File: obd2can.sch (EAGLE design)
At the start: 33 parts, among them Q1 8MHz, SW2 6X3.5_TACT, U1 AP3211KTR-G1, U2 SN65HVD235DR, U3 STM32F072-LQFP48, X1 RJ45_RIGHT_ANGLEMOLEX_95001-2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, X2 RJ45_RIGHT_ANGLEMOLEX_95001-2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

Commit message: combined designs together
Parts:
- removed C25, C28: 22uF, rcl:C-USC1206
- removed C27: 10nF, rcl:C-USC0603
- removed D5: (no value), diode:SCHOTTKY-DIODESMC
- removed L1: 4.7uH, rcl:L-EUL2012C
- removed L2: (no value), wuerth-elektronik:WE-CBF_1812
- removed Q1: 8MHz, SparkFun2:CRYSTAL5X3
- removed SV1: (no value), con-lstb:MA06-1
- removed SW2: 6X3.5_TACT, tactile_switch:6X3.5_TACT
- removed TC2: TC2030-IDC-NL, TagConnect:TC2030-IDC-NL
- removed TP2: TPB1,27, testpad:TPB1,27
- removed X1: RJ45_RIGHT_ANGLEMOLEX_95001-2881, FCI_RJ12:RJ45_RIGHT_ANGLEMOLEX_95001-2881
- added C1, C17, C6: 1uF, SparkFun:CAP0402-CAP
- added C1000: 10uF, rcl:CPOL-USSMCA
- added C10000: 1uf, rcl:C-USC0603K
- added C11000, C13000: 22uF, rcl:C-USC1206
- added C13: 560pF, SparkFun:CAP0402-CAP
- added C16: 470pF, SparkFun:CAP0402-CAP
- added C18: 10uF, SparkFun:CAP_POL1206
- added C19: 10nF, rcl:C-USC0603
- added C2000, C6000, C9000: 0.1uf, rcl:C-USC0603K
- added C3000, C7000: 4.7uf, rcl:C-USC0603K
- added C4: 10uF ESR<=5, SparkFun:CAP_POL1206
- added C4000: 0.01uf, rcl:C-USC0603K
- added C8: 4.7uF, SparkFun:CAP0402-CAP
- added D1000: (no value), diode:SCHOTTKY-DIODESMC
- added D2000: 400V 1A, smt_diodes:DIODE1
- added D3: BAS16, SparkFun:DIODESOD
- added D3000: SCHOTTKY, smt_diodes:SCHOTTKY
- added D4: MBRA140, SparkFun:DIODESMA
- added IC1: SCANTOOL, SparkFun:SCANTOOL
- added IC3: LM339PWR, _stn_logic:LM339PWR
- added IC4: MCP2551, _stn_microchip:MCP2551-I/SN
- added JP1: (no value), SparkFun:M08
- added JP8: DNP, SparkFun:FTDI_BASICPTH
- added JP9: DNP, SparkFun:M02PTH
- added L1000: (no value), wuerth-elektronik:WE-CBF_1812
- added L2000: 4.7uH, rcl:L-EUL2012C
- added LED1, LED3: YELLOW, SparkFun:LED0603
- added LED2, LED4, LED5: RED, SparkFun:LED0603
- added Q10, Q9: BSS138, SparkFun:MOSFET-NCHANNELSMD
- added Q1000: 8MHz, SparkFun2:CRYSTAL5X3
- added Q3, Q4, Q8: MMBT2222, SparkFun:TRANSISTOR_NPNSOT23-3
- added Q7: ZXMP6A13FTA, SparkFun:MOSFET-PCHANNEL
- added R10, R12, R18, R21, R27, R28, R29, R30, R31, R33, R9: 10k, SparkFun:RESISTOR0402-RES
- added R1000: 120, rcl:R-US_R0603
- added R11, R8: 510 0.5W, _stn_rcl:R-US_2010
- added R13, R32, R7: 1k, SparkFun:RESISTOR0402-RES
- added R14, R15: 100, SparkFun:RESISTOR0402-RES
- added R16, R23, R25: 4.7k, SparkFun:RESISTOR0402-RES
- added R17: 1.2k, SparkFun:RESISTOR0402-RES
- added R19: 866, SparkFun:RESISTOR0402-RES
- added R20: 240, SparkFun:RESISTOR0402-RES
- added R22: 374, SparkFun:RESISTOR0402-RES
- added R24, R34: 1.5k, SparkFun:RESISTOR0402-RES
- added R26, R5000: 4.7K, rcl:R-US_R0603
- added R3000: 49.9K 1%, rcl:R-US_R0603
- added R35, R37: 330, SparkFun:RESISTOR0402-RES
- added R4000: 16.2K 1%, rcl:R-US_R0603
- added R6: 10K, SparkFun:RESISTOR0402-RES
- added SV1000: (no value), con-lstb:MA06-1
- added SW1: 6X3.5_TACT, tactile_switch:6X3.5_TACT
- added TC1000: TC2030-IDC-NL, TagConnect:TC2030-IDC-NL
- added U1000: SN65HVD235DR, can:MCP2551SO8
- added U2000: STM32F072-LQFP48, stm32f0:STM32F072-LQFP48
- added U3000: AP3211KTR-G1, diodes_inc:AP3211KTR-G1
- added X1000, X2000: RJ45_RIGHT_ANGLEMOLEX_95001-2881, FCI_RJ12:RJ45_RIGHT_ANGLEMOLEX_95001-2881
- added Y1: 16MHz, SparkFun:CRYSTAL5X3
- C10: value 1uf -> 0.1uF; device rcl:C-USC0603K -> SparkFun:CAP0402-CAP
- C11: value 0.01uf -> 1uF; device rcl:C-USC0603K -> SparkFun:CAP0402-CAP
- C12: value 4.7uf -> 560pF; device rcl:C-USC0603K -> SparkFun:CAP0402-CAP
- C14: value 0.1uf -> 0.1uF; device rcl:C-USC0603K -> SparkFun:CAP0402-CAP
- C15: value 4.7uf -> 2.2uF; device rcl:C-USC0603K -> SparkFun:CAP0402-CAP
- C2, C3: value 33pF -> 27pF; device SparkFun:CAP0603 -> SparkFun:CAP0402-CAP
- C5: value 0.1uf -> 1uF; device rcl:C-USC0603K -> SparkFun:CAP0402-CAP
- C7: value 10uF -> 0.1uF; device rcl:CPOL-USSMCA -> SparkFun:CAP0402-CAP
- C9: value 0.1uf -> 10uF; device rcl:C-USC0603K -> SparkFun:CAP_POL1206
- D1: value SCHOTTKY -> BAS16; device smt_diodes:SCHOTTKY -> SparkFun:DIODESOD
- D2: value 400V 1A -> BAS16; device smt_diodes:DIODE1 -> SparkFun:DIODESOD
- R1: value 4.7K -> 10k; device rcl:R-US_R0603 -> SparkFun:RESISTOR0402-RES
- R2: value 120 -> 1k; device rcl:R-US_R0603 -> SparkFun:RESISTOR0402-RES
- R3: value 16.2K 1% -> 62K; device rcl:R-US_R0603 -> SparkFun:RESISTOR0402-RES
- R4: value 49.9K 1% -> 330; device rcl:R-US_R0603 -> SparkFun:RESISTOR0402-RES
- R5: value 4.7K -> 330; device rcl:R-US_R0603 -> SparkFun:RESISTOR0402-RES
- U1: value AP3211KTR-G1 -> 3.3V; device diodes_inc:AP3211KTR-G1 -> SparkFun:V_REG_LDOSMD
- U2: value SN65HVD235DR -> V_REG_317DPACK; device can:MCP2551SO8 -> SparkFun:V_REG_317DPACK
- U3: value STM32F072-LQFP48 -> 5V Reg.; device stm32f0:STM32F072-LQFP48 -> SparkFun:V_REG_LDOSMD
- X2: value RJ45_RIGHT_ANGLEMOLEX_95001-2881 -> Male DB9; device FCI_RJ12:RJ45_RIGHT_ANGLEMOLEX_95001-2881 -> SparkFun:DB9MALE
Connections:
- new net !ISO_K_TX: IC1.!ISO_K_TX, R13.2
- new net !ISO_L_TX: IC1.!ISO_L_TX, R7.2
- new net !ISO_RX: IC1.!ISO_RX, IC3B.OUT, R9.1
- new net !OBD_RX_STATUS!/PGC: IC1.!OBD_RX_LED!/!INT, R4.1
- new net !PWR_SAVE: IC1.PWR_CTRL
- new net !VPW_RX: IC1.!VPW_RX, IC3C.OUT, R18.1
- new net 3.3V: C1.1, C5.1, C8.1, IC1.AVDD, IC1.VDD, LED1.A, LED2.A, LED3.A, LED4.A, R18.2, R27.2, R9.2, U1.OUT
- new net 5V: C11.1, C15.1, C18.+, C6.1, D3.A, IC4.VDD, R1.2, R17.2, R25.1, R34.1, U1.EN, U1.IN, U3.OUT
- new net BATT_V: C7.1, IC1.ANALOG_IN, R3.1, R6.2
- new net CAN_HI: IC4.CANH, JP1.6, R14.2, X2.3
- new net CAN_LO: IC4.CANL, JP1.7, R15.2, X2.5
- new net HOST_PRESENT: IC1.!SLEEP
- new net J1850BUS+: D1.C, JP1.3, R21.1, R28.1, R30.1, X2.7
- new net J1850BUS+_TX: IC1.J1850_BUS+_TX, Q9.G
- new net J1850BUS-: JP1.2, Q8.C, R29.1, R31.2, X2.6
- new net J1850BUS-_TX: IC1.!J1850_BUS-_TX, R32.1
- new net K-LINE: JP1.5, Q4.C, R11.2, R12.1, X2.4
- new net L-LINE: JP1.4, Q3.C, R8.2, X2.8
- new net N$10: C12.1, R14.1
- new net N$11: IC4.RS, R16.2
- new net N$12: IC3C.+IN, R17.1, R23.2
- new net N$13: IC3B.-IN, R12.2
- new net N$14: D3.C, R31.1
- new net N$15: R26.2, U1000G$1.RS
- new net N$16: R3000.2, R4000.1, U3000.FB
- new net N$17: C19.2, U3000.BS
- new net N$18: Q7.G, Q9.D, R24.2
- new net N$19: C19.1, D3000.C, L2000.1, U3000.SW
- new net N$22: Q10.D, R19.1, R22.2
- new net N$24: D2.A, R30.2
- new net N$25: Q8.B, R32.2
- new net N$26: C4.+, IC1.VCAP
- new net N$27: C13.1, R15.1
- new net N$30: LED3.C, R4.2
- new net N$31: LED4.C, R5.1
- new net N$32: LED5.A, R2.1
- new net N$35: LED1.C, R35.2
- new net N$36: LED2.C, R37.1
- new net N$4: Q4.B, R13.1
- new net N$7: IC3C.-IN, R21.2
- new net N$8: R19.2, R20.2, U2.ADJ
- new net N$9: D1.A, Q7.D
- new net OSC1: C2.1, IC1.OSC1, Y1.2
- new net OSC2: C3.1, IC1.OSC2, Y1.1
- new net PWM/!VPW: IC1.PWM/!VPW, Q10.G
- new net PWM_RX: IC1.PWM_RX, IC3A.OUT, R27.1
- new net RST_NVM: IC1.!OBD_TX_LED!/!RST_NVM, JP9.1, R5.2
- new net RX-I: IC1.UART_RX, JP8.3
- new net RX-STAT: IC1.!UART_RX_LED, R35.1
- new net TX-O: IC1.UART_TX, JP8.2, R25.2
- new net TX-STAT: IC1.!UART_TX_LED, R37.2
- new net VBAT: C14.1, D4.C, IC3P.VCC, JP1.8, R10.1, R11.1, R8.1, U2.IN
- new net VBATT_RAW: D4.A, R3.2, X2.9
- new net VCC: C10.1, C17.1, C9.+, Q7.S, R2.2, R20.1, R24.1, U2.OUT, U3.EN, U3.IN
- net +12V: now also L1000.2, X1000.P8, X2000.P8; no longer L2.2, X1.P8, X2.P8
- net +5V: now also SV1000.3; no longer SV1.3
- net AGND: now also U2000.VSSA(P8); no longer U3.VSSA(P8)
- net ANALOG_1_ADC: now also U2000.PA0/USART4_TX/WKUP1/ADC_IN0; no longer U3.PA0/USART4_TX/WKUP1/ADC_IN0
- net CANH: now also R1000.1, U1000G$1.CANH, X1000.P2; no longer R2.1, U2G$1.CANH, X1.P2
- net CANL: now also R1000.2, U1000G$1.CANL, X1000.P3; no longer R2.2, U2G$1.CANL, X1.P3
- net CAN_RX: now also IC1.CAN_RX, IC4.ROUT, U1000G$1.RXD, U2000.PA11/USB_DM/CAN_RX; no longer U2G$1.RXD, U3.PA11/USB_DM/CAN_RX
- net CAN_TX: now also IC1.CAN_TX, IC4.TIN, R34.2, U1000G$1.TXD, U2000.PA12/USB_DP/CAN_TX; no longer U2G$1.TXD, U3.PA12/USB_DP/CAN_TX
- net GND: now also C1.2, C1000.-, C10000.2, C11000.2, C13.2, C13000.2, C16.2, C17.2, C18.-, C2.2, C2000.2, C3.2, C3000.2, C4.-, C4000.2, C6.2, C6000.2, C7.2, C7000.2, C8.2, C9.-, C9000.2, D1000.A, D2.C, D3000.A, IC1.AVSS, IC1.PAD, IC1.VSS@16, IC1.VSS@5, IC3P.GND, IC4.VSS, JP1.1, JP8.6, JP9.2, LED5.C, Q10.S, Q3.E, Q4.E, Q8.E, Q9.S, R16.1, R22.1, R23.1, R26.1, R33.2, R4000.2, R6.1, SV1000.1, SW1.2, TC1000.5, U1000G$1.VREF, U1000G$2.GND, U2000.BOOT0(P44), U2000.VSS_1(P23), U2000.VSS_2(P35), U2000.VSS_3(P47), U3.GND, U3000.GND, X1000.P1, X2.1, X2.2, X2000.P1; no longer C2.1, C25.2, C28.2, C3.1, C7.-, C9.2, D1.A, D5.A, R1.1, R3.2, SV1.1, SW2.2, TC2.5, U2G$1.VREF, U2G$2.GND, U3.BOOT0(P44), U3.VSS_1(P23), U3.VSS_2(P35), U3.VSS_3(P47), X1.P1, X2.P1
- net N$1: now also IC3A.+IN, R28.2; no longer R3.1, R4.2, U1.FB
- net N$3: now also IC3A.-IN, R29.2; no longer TP2.TP, U3.PB0/ADC_IN8/TIM3_CH3
- net N$34: now also C16.1, U3.BP; no longer R1.2, U2G$1.RS
- net N$40: now also Q1000.2, U2000.PF1/OSC_OUT; no longer C2.2, Q1.2, U3.PF1/OSC_OUT
- net N$42: now also Q1000.1, U2000.PF0/OSC_IN; no longer C3.2, Q1.1, U3.PF0/OSC_IN
- net N$5: now also Q3.B, R7.1; no longer C27.2, U1.BS
- net N$50: now also D2000.A, L1000.1; no longer D2.A, L2.1
- net N$6: now also IC3B.+IN, R10.2, R33.1; no longer C27.1, D1.C, L1.1, U1.SW
- net RESET: now also IC1.!RESET, R1.1, R5000.1, SW1.1, TC1000.3, U2000.NRST(P7); no longer R5.1, SW2.1, TC2.3, U3.NRST(P7)
- net SAFE12V: now also C11000.1, D1000.C, D2000.C, U3000.EN, U3000.IN; no longer C25.1, D2.C, D5.C, U1.EN, U1.IN
- net SWCLK: now also TC1000.4, U2000.PA14/USART2_TX/SWCLK; no longer TC2.4, U3.PA14/USART2_TX/SWCLK
- net SWDIO: now also TC1000.2, U2000.PA13/SWDIO; no longer TC2.2, U3.PA13/SWDIO
- net U3: now also R3000.1, R5000.2, TC1000.1; no longer R4.1, R5.2, TC2.1
- net USART1_RX: now also SV1000.4, U2000.PA10/USART1_RX/TIM1_CH3; no longer SV1.4, U3.PA10/USART1_RX/TIM1_CH3
- net USART1_TX: now also SV1000.5, U2000.PA9/USART1_TX/TIM1_CH2; no longer SV1.5, U3.PA9/USART1_TX/TIM1_CH2
- net USART2_RX: now also U2000.PA3/ADC_IN3/COMP2_INP/USART2_RX; no longer U3.PA3/ADC_IN3/COMP2_INP/USART2_RX
- net USART2_TX: now also U2000.PA2/ADC_IN2/WKUP4USART2_TX; no longer U3.PA2/ADC_IN2/WKUP4USART2_TX
- net V+: now also C1000.+, C10000.1, C13000.1, C2000.1, C3000.1, C4000.1, C6000.1, C7000.1, C9000.1, L2000.2, U1000G$2.VCC, U2000.VBATT(P1), U2000.VDDA(P9), U2000.VDDIO2(P36), U2000.VDD_1(P24), U2000.VDD_2(P48); no longer C10.1, C11.1, C12.1, C14.1, C15.1, C28.1, C5.1, C7.+, C9.1, L1.2, U2G$2.VCC, U3.VBATT(P1), U3.VDDA(P9), U3.VDDIO2(P36), U3.VDD_1(P24), U3.VDD_2(P48)
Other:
- note added: "+3.3V Power Supply"
- note added: "AVSS"
- note added: "CAN Transceiver"
- note added: "CAP-868"
- note added: "ISO Transceiver"
- note added: "J1850 Transceiver"
- note added: "Main Controller"
- note added: "New Part: LM339"
- note added: "New Parts: 866, 374"
- note added: "Selectable 5.76V or 7.71V"

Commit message: label adjustment, snapshot image
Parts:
- removed C1000: 10uF, rcl:CPOL-USSMCA
- removed C10000: 1uf, rcl:C-USC0603K
- removed C11000, C13000: 22uF, rcl:C-USC1206
- removed C2000, C6000, C9000: 0.1uf, rcl:C-USC0603K
- removed C3000, C7000: 4.7uf, rcl:C-USC0603K
- removed C4000: 0.01uf, rcl:C-USC0603K
- removed D1000: (no value), diode:SCHOTTKY-DIODESMC
- removed IC3: LM339PWR, _stn_logic:LM339PWR
- removed IC4: MCP2551, _stn_microchip:MCP2551-I/SN
- removed JP1: (no value), SparkFun:M08
- removed JP8: DNP, SparkFun:FTDI_BASICPTH
- removed JP9: DNP, SparkFun:M02PTH
- removed LED4, LED5: RED, SparkFun:LED0603
- removed Q1000: 8MHz, SparkFun2:CRYSTAL5X3
- removed Q9: BSS138, SparkFun:MOSFET-NCHANNELSMD
- removed R1000: 120, rcl:R-US_R0603
- removed R3000: 49.9K 1%, rcl:R-US_R0603
- removed R33: 10k, SparkFun:RESISTOR0402-RES
- removed R34: 1.5k, SparkFun:RESISTOR0402-RES
- removed R35, R37: 330, SparkFun:RESISTOR0402-RES
- removed R4000: 16.2K 1%, rcl:R-US_R0603
- removed R5000: 4.7K, rcl:R-US_R0603
- removed U1000: SN65HVD235DR, can:MCP2551SO8
- removed U3000: AP3211KTR-G1, diodes_inc:AP3211KTR-G1
- removed X2000: RJ45_RIGHT_ANGLEMOLEX_95001-2881, FCI_RJ12:RJ45_RIGHT_ANGLEMOLEX_95001-2881
- added C20, C23: 10uF, SparkFun:CAP_POL1206
- added C21: 2.2uF, SparkFun:CAP0402-CAP
- added C22: 470pF, SparkFun:CAP0402-CAP
- added C24: 0.1uF, SparkFun:CAP0402-CAP
- added IC2: SCANTOOL, SparkFun:SCANTOOL
- added Q5, Q6: MMBT2222, SparkFun:TRANSISTOR_NPNSOT23-3
- added U5: 5V Reg., SparkFun:V_REG_LDOSMD
- C1, C6: value 1uF -> 0.1uF
- C10: value 0.1uF -> 0.1uf; device SparkFun:CAP0402-CAP -> rcl:C-USC0603K
- C11: value 1uF -> 10uF; device SparkFun:CAP0402-CAP -> rcl:CPOL-USSMCA
- C12: value 560pF -> 4.7uf; device SparkFun:CAP0402-CAP -> rcl:C-USC0603K
- C13: value 560pF -> 0.01uf; device SparkFun:CAP0402-CAP -> rcl:C-USC0603K
- C14: value 0.1uF -> 22uF; device SparkFun:CAP0402-CAP -> rcl:C-USC1206
- C15: value 2.2uF -> 10nF; device SparkFun:CAP0402-CAP -> rcl:C-USC0603
- C16: value 470pF -> 0.1uf; device SparkFun:CAP0402-CAP -> rcl:C-USC0603K
- C17: value 1uF -> 4.7uf; device SparkFun:CAP0402-CAP -> rcl:C-USC0603K
- C18: value 10uF -> 22uF; device SparkFun:CAP_POL1206 -> rcl:C-USC1206
- C19: value 10nF -> 1uf; device rcl:C-USC0603 -> rcl:C-USC0603K
- C2: value 27pF -> 1uF
- C7: value 0.1uF -> 27pF
- C8: value 4.7uF -> 1uF
- C9: value 10uF -> 0.1uf; device SparkFun:CAP_POL1206 -> rcl:C-USC0603K
- D4: value MBRA140 -> (none); device SparkFun:DIODESMA -> diode:SCHOTTKY-DIODESMC
- IC1: value SCANTOOL -> LM339PWR; device SparkFun:SCANTOOL -> _stn_logic:LM339PWR
- LED3: value YELLOW -> RED
- Q3: value MMBT2222 -> ZXMP6A13FTA; device SparkFun:TRANSISTOR_NPNSOT23-3 -> SparkFun:MOSFET-PCHANNEL
- Q4: value MMBT2222 -> BSS138; device SparkFun:TRANSISTOR_NPNSOT23-3 -> SparkFun:MOSFET-NCHANNELSMD
- Q7: value ZXMP6A13FTA -> 8MHz; device SparkFun:MOSFET-PCHANNEL -> SparkFun2:CRYSTAL5X3
- R1: value 10k -> 10K
- R10: value 10k -> 374
- R11: value 510 0.5W -> 330; device _stn_rcl:R-US_2010 -> SparkFun:RESISTOR0402-RES
- R13: value 1k -> 1.2k
- R14: value 100 -> 866
- R15: value 100 -> 10k
- R16: value 4.7k -> 240
- R17: value 1.2k -> 10k
- R19: value 866 -> 10k
- R2: value 1k -> 62K
- R20: value 240 -> 120; device SparkFun:RESISTOR0402-RES -> rcl:R-US_R0603
- R21, R27, R28, R9: value 10k -> 1k
- R22: value 374 -> 10k
- R23: value 4.7k -> 10k
- R25: value 4.7k -> 4.7K; device SparkFun:RESISTOR0402-RES -> rcl:R-US_R0603
- R26: value 4.7K -> 510 0.5W; device rcl:R-US_R0603 -> _stn_rcl:R-US_2010
- R29: value 10k -> 49.9K 1%; device SparkFun:RESISTOR0402-RES -> rcl:R-US_R0603
- R3: value 62K -> 10k
- R30: value 10k -> 16.2K 1%; device SparkFun:RESISTOR0402-RES -> rcl:R-US_R0603
- R31: value 10k -> 4.7K; device SparkFun:RESISTOR0402-RES -> rcl:R-US_R0603
- R32: value 1k -> 510 0.5W; device SparkFun:RESISTOR0402-RES -> _stn_rcl:R-US_2010
- R4, R5: value 330 -> 10k
- R6: value 10K -> 10k
- R7: value 1k -> 330
- R8: value 510 0.5W -> 4.7k; device _stn_rcl:R-US_2010 -> SparkFun:RESISTOR0402-RES
- U1: value 3.3V -> V_REG_317DPACK; device SparkFun:V_REG_LDOSMD -> SparkFun:V_REG_317DPACK
- U2: value V_REG_317DPACK -> SN65HVD235DR; device SparkFun:V_REG_317DPACK -> can:MCP2551SO8
- U3: value 5V Reg. -> AP3211KTR-G1; device SparkFun:V_REG_LDOSMD -> diodes_inc:AP3211KTR-G1
- X2: value Male DB9 -> RJ45_RIGHT_ANGLEMOLEX_95001-2881; device SparkFun:DB9MALE -> FCI_RJ12:RJ45_RIGHT_ANGLEMOLEX_95001-2881
- renumbered D2000 to D5, D3000 to D6, L1000 to L1, L2000 to L2, Q10 to Q1, Q8 to Q2, SV1000 to SV1, TC1000 to TC1, U2000 to U4, X1000 to X1
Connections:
- removed net 3.3V: C1.1, C5.1, C8.1, IC1.AVDD, IC1.VDD, LED1.A, LED2.A, LED3.A, LED4.A, R18.2, R27.2, R9.2, U1.OUT
- removed net CAN_HI: IC4.CANH, JP1.6, R14.2, X2.3
- removed net CAN_LO: IC4.CANL, JP1.7, R15.2, X2.5
- removed net N$10: C12.1, R14.1
- removed net N$11: IC4.RS, R16.2
- removed net N$27: C13.1, R15.1
- removed net N$35: LED1.C, R35.2
- removed net N$36: LED2.C, R37.1
- removed net RX-I: IC1.UART_RX, JP8.3
- removed net RX-STAT: IC1.!UART_RX_LED, R35.1
- removed net TX-O: IC1.UART_TX, JP8.2, R25.2
- removed net TX-STAT: IC1.!UART_TX_LED, R37.2
- removed net USART2_RX: U4.PA3/ADC_IN3/COMP2_INP/USART2_RX
- removed net USART2_TX: U4.PA2/ADC_IN2/WKUP4USART2_TX
- removed net VBAT: C14.1, D4.C, IC3P.VCC, JP1.8, R10.1, R11.1, R8.1, U2.IN
- removed net VBATT_RAW: D4.A, R3.2, X2.9
- new net RESET_STN: IC2.!RESET
- new net RX_FROM_STN: IC2.UART_TX, U4.PA3/ADC_IN3/COMP2_INP/USART2_RX
- new net TX_TO_STN: IC2.UART_RX, U4.PA2/ADC_IN2/WKUP4USART2_TX
- net !ISO_K_TX: now also IC2.!ISO_K_TX, R28.2; no longer IC1.!ISO_K_TX, R13.2
- net !ISO_L_TX: now also IC2.!ISO_L_TX, R27.2; no longer IC1.!ISO_L_TX, R7.2
- net !ISO_RX: now also IC1B.OUT, IC2.!ISO_RX, R4.1; no longer IC1.!ISO_RX, IC3B.OUT, R9.1
- net !OBD_RX_STATUS!/PGC: now also IC2.!OBD_RX_LED!/!INT, R7.1; no longer IC1.!OBD_RX_LED!/!INT, R4.1
- net !PWR_SAVE: now also IC2.PWR_CTRL; no longer IC1.PWR_CTRL
- net !VPW_RX: now also IC1C.OUT, IC2.!VPW_RX, R5.1; no longer IC1.!VPW_RX, IC3C.OUT, R18.1
- net +12V: now also R2.2, X2.P8; no longer X2000.P8
- net 5V: now also C20.+, C21.1, D1.A, R13.2, U5.OUT; no longer C11.1, C15.1, C18.+, C6.1, D3.A, IC4.VDD, R1.2, R17.2, R25.1, R34.1, U1.EN, U1.IN, U3.OUT
- net BATT_V: now also C1.1, IC2.ANALOG_IN, R1.2, R2.1; no longer C7.1, IC1.ANALOG_IN, R3.1, R6.2
- net CANH: now also R20.1, U2G$1.CANH; no longer R1000.1, U1000G$1.CANH
- net CANL: now also R20.2, U2G$1.CANL; no longer R1000.2, U1000G$1.CANL
- net CAN_RX: now also U2G$1.RXD; no longer IC1.CAN_RX, IC4.ROUT, U1000G$1.RXD
- net CAN_TX: now also U2G$1.TXD; no longer IC1.CAN_TX, IC4.TIN, R34.2, U1000G$1.TXD
- net GND: now also C11.-, C18.2, C19.2, C20.-, C21.2, C22.2, C23.-, C24.2, C9.2, D4.A, IC1P.GND, IC2.AVSS, IC2.PAD, IC2.VSS@16, IC2.VSS@5, LED2.C, Q4.S, Q5.E, Q6.E, R1.1, R10.1, R15.2, R25.1, R30.2, R8.1, U2G$1.VREF, U2G$2.GND, U5.GND, X2.P1; no longer C1000.-, C10000.2, C11.2, C11000.2, C13000.2, C15.2, C18.-, C2000.2, C3000.2, C4000.2, C6000.2, C7000.2, C9.-, C9000.2, D1000.A, IC1.AVSS, IC1.PAD, IC1.VSS@16, IC1.VSS@5, IC3P.GND, IC4.VSS, JP1.1, JP8.6, JP9.2, LED5.C, Q3.E, Q4.E, Q9.S, R16.1, R22.1, R23.1, R26.1, R33.2, R4000.2, R6.1, U1.GND, U1000G$1.VREF, U1000G$2.GND, U3000.GND, X2.1, X2.2, X2000.P1
- net HOST_PRESENT: now also IC2.!SLEEP; no longer IC1.!SLEEP
- net J1850BUS+: now also D3.C, R18.1, R19.1, R23.1, X2.P4; no longer D1.C, JP1.3, R21.1, R28.1, R30.1, X2.7
- net J1850BUS+_TX: now also IC2.J1850_BUS+_TX, Q4.G; no longer IC1.J1850_BUS+_TX, Q9.G
- net J1850BUS-: now also R17.1, R22.2, X2.P5; no longer JP1.2, R29.1, R31.2, X2.6
- net J1850BUS-_TX: now also IC2.!J1850_BUS-_TX, R21.1; no longer IC1.!J1850_BUS-_TX, R32.1
- net K-LINE: now also Q6.C, R32.2, R6.1, X2.P7; no longer JP1.5, Q4.C, R11.2, R12.1, X2.4
- net L-LINE: now also Q5.C, R26.2, X2.P6; no longer JP1.4, Q3.C, R8.2, X2.8
- net N$1: now also IC1A.+IN, R18.2; no longer IC3A.+IN, R28.2
- net N$12: now also IC1C.+IN, R13.1, R8.2; no longer IC3C.+IN, R17.1, R23.2
- net N$13: now also IC1B.-IN, R6.2; no longer IC3B.-IN, R12.2
- net N$14: now also D1.C, R22.1; no longer D3.C, R31.1
- net N$15: now also R25.2, U2G$1.RS; no longer R26.2, U1000G$1.RS
- net N$16: now also R29.2, R30.1, U3.FB; no longer R3000.2, R4000.1, U3000.FB
- net N$17: now also C15.2, U3.BS; no longer C19.2, U3000.BS
- net N$18: now also Q3.G, Q4.D; no longer Q7.G, Q9.D
- net N$19: now also C15.1, U3.SW; no longer C19.1, U3000.SW
- net N$22: now also R10.2, R14.1; no longer R19.1, R22.2
- net N$24: now also R23.2; no longer R30.2
- net N$25: now also R21.2; no longer R32.2
- net N$26: now also IC2.VCAP; no longer IC1.VCAP
- net N$3: now also IC1A.-IN, R17.2; no longer IC3A.-IN, R29.2
- net N$30: now also LED1.C, R7.2; no longer LED3.C, R4.2
- net N$31: now also LED3.C, R11.1; no longer LED4.C, R5.1
- net N$32: now also LED2.A, R9.1; no longer LED5.A, R2.1
- net N$34: now also C22.1, U5.BP; no longer C16.1, U3.BP
- net N$4: now also Q6.B, R28.1; no longer Q4.B, R13.1
- net N$40: now also Q7.2; no longer Q1000.2
- net N$42: now also Q7.1; no longer Q1000.1
- net N$5: now also Q5.B, R27.1; no longer Q3.B, R7.1
- net N$6: now also IC1B.+IN, R12.2, R15.1; no longer IC3B.+IN, R10.2, R33.1
- net N$7: now also IC1C.-IN, R19.2; no longer IC3C.-IN, R21.2
- net N$8: now also R14.2, R16.2, U1.ADJ; no longer R19.2, R20.2, U2.ADJ
- net N$9: now also D3.A, Q3.D; no longer D1.A, Q7.D
- net OSC1: now also C3.1, IC2.OSC1; no longer C2.1, IC1.OSC1
- net OSC2: now also C7.1, IC2.OSC2; no longer C3.1, IC1.OSC2
- net PWM/!VPW: now also IC2.PWM/!VPW; no longer IC1.PWM/!VPW
- net PWM_RX: now also IC1A.OUT, IC2.PWM_RX, R3.1; no longer IC1.PWM_RX, IC3A.OUT, R27.1
- net RESET: now also R31.1; no longer IC1.!RESET, R1.1, R5000.1
- net RST_NVM: now also IC2.!OBD_TX_LED!/!RST_NVM, R11.2; no longer IC1.!OBD_TX_LED!/!RST_NVM, JP9.1, R5.2
- net SAFE12V: now also C14.1, C6.1, D4.C, IC1P.VCC, R12.1, R26.1, R32.1, U1.IN, U3.EN, U3.IN; no longer C11000.1, D1000.C, U3000.EN, U3000.IN
- net U3: now also R29.1, R31.2; no longer R3000.1, R5000.2
- net V+: now also C10.1, C11.+, C12.1, C13.1, C16.1, C17.1, C18.1, C19.1, C2.1, C8.1, C9.1, IC2.AVDD, IC2.VDD, LED1.A, LED3.A, R3.2, R4.2, R5.2, U2G$2.VCC; no longer C1000.+, C10000.1, C13000.1, C2000.1, C3000.1, C4000.1, C6000.1, C7000.1, C9000.1, U1000G$2.VCC
- net VCC: now also C23.+, C24.1, C5.1, Q3.S, R16.1, R9.2, U1.OUT, U5.EN, U5.IN; no longer C10.1, C17.1, C9.+, Q7.S, R2.2, R20.1, U2.OUT, U3.EN, U3.IN
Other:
- note removed: "CAN Transceiver"

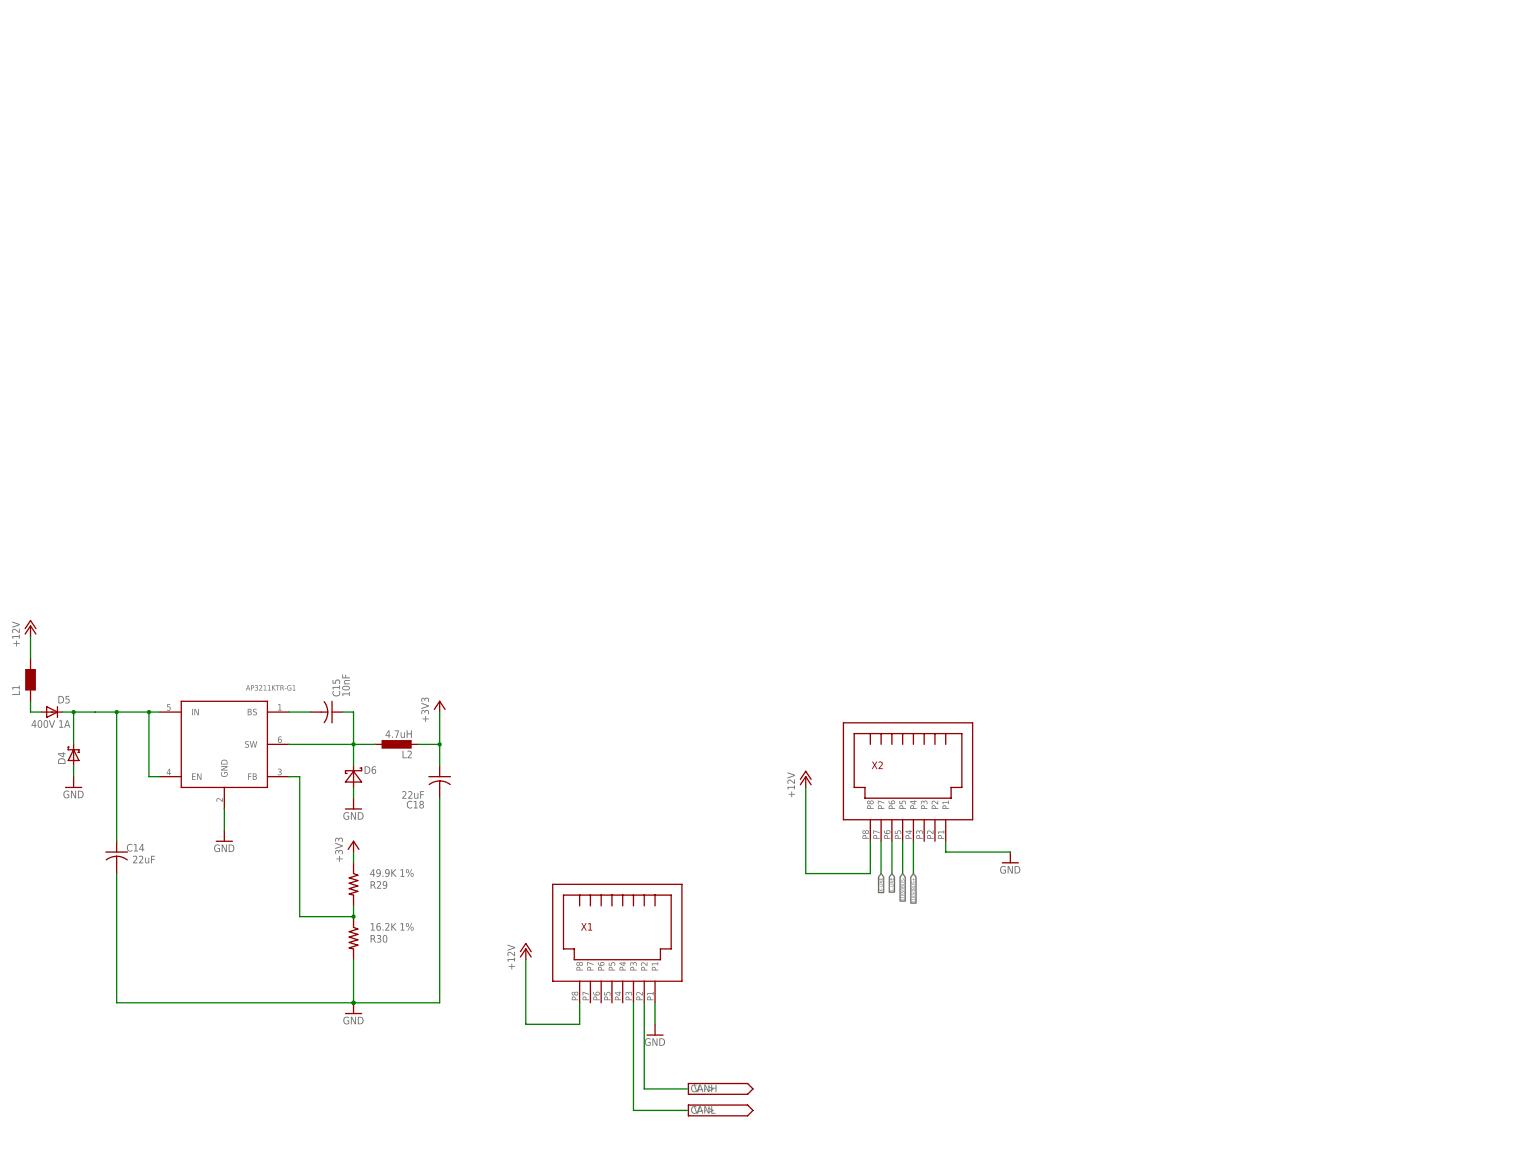
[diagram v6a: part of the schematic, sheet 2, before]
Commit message: OBD2CAN WIP - more air wires routed
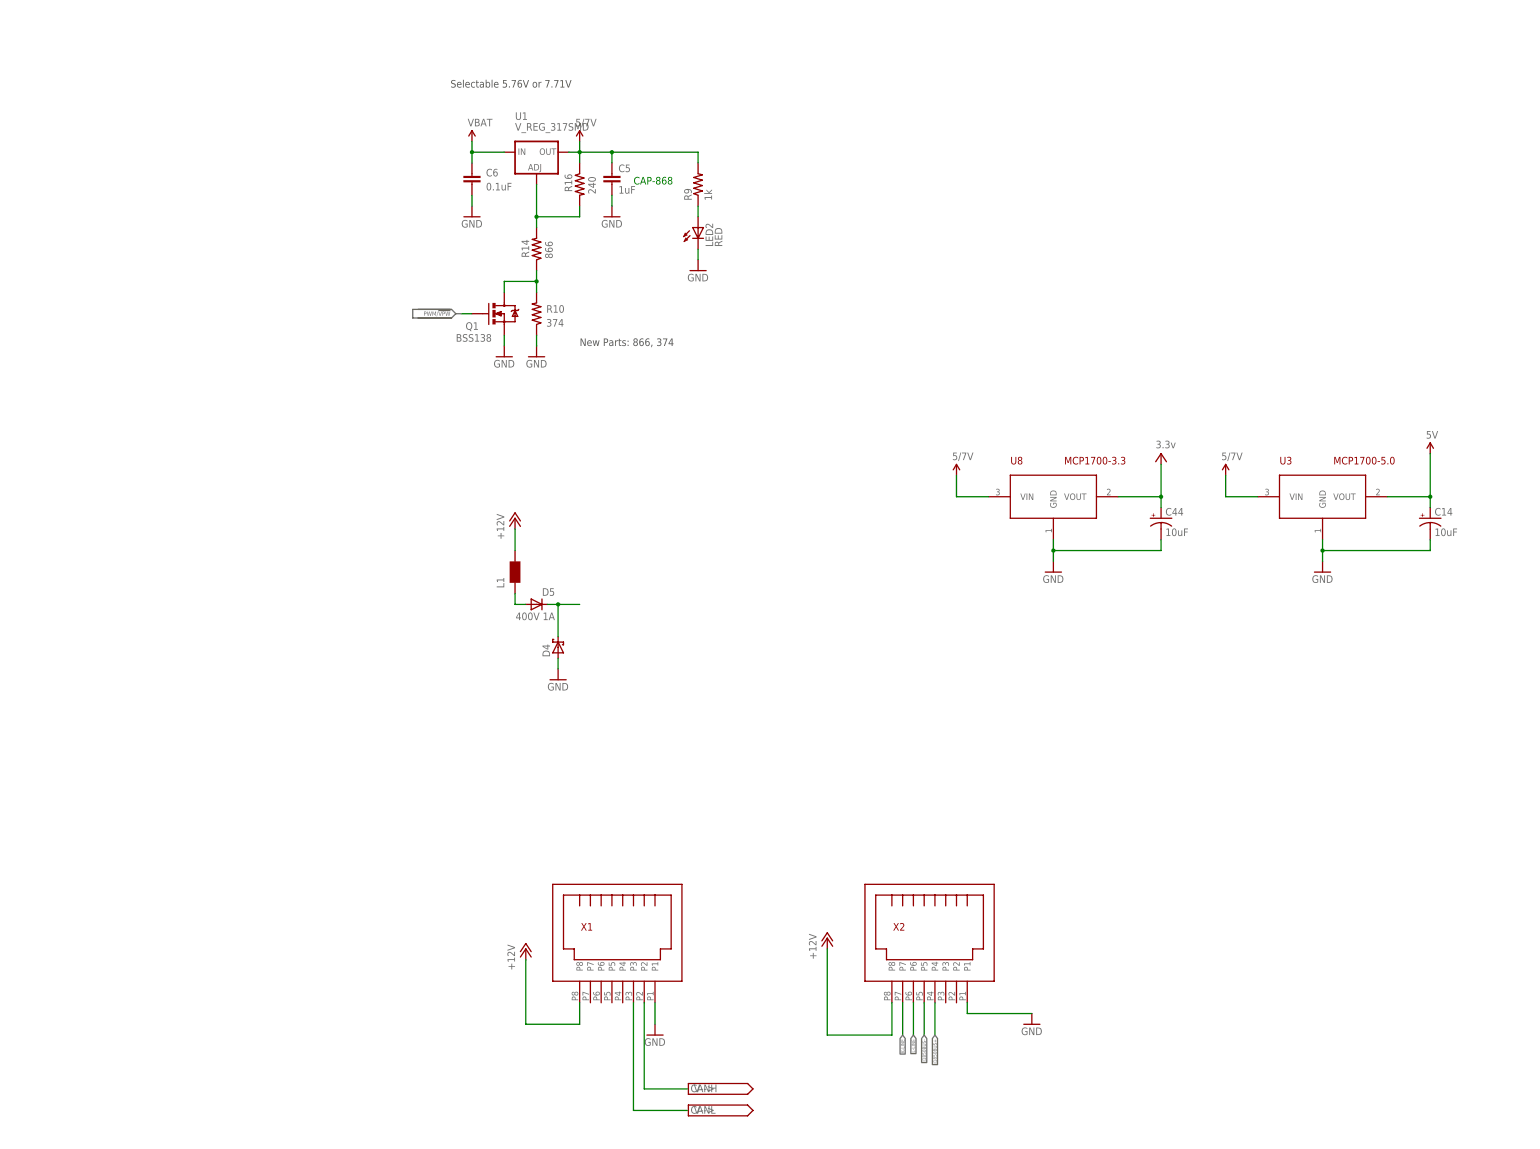
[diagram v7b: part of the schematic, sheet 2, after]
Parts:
- removed C15: 10nF, rcl:C-USC0603
- removed C18: 22uF, rcl:C-USC1206
- removed C20, C23: 10uF, SparkFun:CAP_POL1206
- removed C21: 2.2uF, SparkFun:CAP0402-CAP
- removed C22: 470pF, SparkFun:CAP0402-CAP
- removed C24: 0.1uF, SparkFun:CAP0402-CAP
- removed D6: SCHOTTKY, smt_diodes:SCHOTTKY
- removed L2: 4.7uH, rcl:L-EUL2012C
- removed R29: 49.9K 1%, rcl:R-US_R0603
- removed R30: 16.2K 1%, rcl:R-US_R0603
- removed U5: 5V Reg., SparkFun:V_REG_LDOSMD
- added C44: 10uF, rcl:CPOL-USSMCA
- added U8: MCP1700-3.3, mcp1700:MCP1700
- C14: value 22uF -> 10uF; device rcl:C-USC1206 -> rcl:CPOL-USSMCA
- U1: value V_REG_317DPACK -> V_REG_317SMD; device SparkFun:V_REG_317DPACK -> SparkFun:V_REG_317SMD
- U3: value AP3211KTR-G1 -> MCP1700-5.0; device diodes_inc:AP3211KTR-G1 -> mcp1700:MCP1700
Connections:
- removed net N$16: R29.2, R30.1, U3.FB
- removed net N$17: C15.2, U3.BS
- removed net N$19: C15.1, D6.C, L2.1, U3.SW
- removed net N$34: C22.1, U5.BP
- removed net U3: R29.1, R31.2, TC1.1
- net 5V: now also C14.+, U3.VOUT; no longer C20.+, C21.1, U5.OUT
- net GND: now also C14.-, C44.-, U8.GND; no longer C14.2, C18.2, C20.-, C21.2, C22.2, C23.-, C24.2, D6.A, R30.2, U5.GND
- net SAFE12V: no longer C14.1, U3.EN, U3.IN
- net V+: now also C44.+, R31.2, TC1.1, U8.VOUT; no longer C18.1, L2.2
- net VCC: now also U3.VIN, U8.VIN; no longer C23.+, C24.1, U5.EN, U5.IN
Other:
- moved on the sheet: D4, D5, L1, X2

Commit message: fully routed; passes DRC and ERC
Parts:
- removed LED2: RED, SparkFun:LED0603
- removed R9: 1k, SparkFun:RESISTOR0402-RES
- added ACT, POWER: PANEL_LED, LEDs:PANEL_LED
- added ACT_S, POWER_S: (no value), led:LEDCHIPLED_0603
- added C15, C18: 0.1uf, rcl:C-USC0603K
- added R29, R30: 180, SparkFun:RESISTOR0402-RES
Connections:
- removed net AGND: U4.VSSA(P8)
- removed net N$32: LED2.A, R9.1
- new net GND1: ACT.C, ACT_S.C, R29.1
- new net GND2: POWER.C, POWER_S.C, R30.1
- new net N$11: R29.2, U4.PB12
- net GND: now also C15.1, C18.1, R30.2, U4.VSSA(P8); no longer LED2.C
- net N$40: now also C18.2
- net N$42: now also C15.2
- net RESET_STN: now also U4.PB2
- net V+: now also ACT.A, ACT_S.A, POWER.A, POWER_S.A
- net VCC: no longer R9.2
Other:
- note removed: "+3.3V Power Supply"
